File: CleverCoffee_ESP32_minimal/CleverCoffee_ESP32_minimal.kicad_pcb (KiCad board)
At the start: 2 copper layers, 78.2 x 57.5 mm, 24 parts

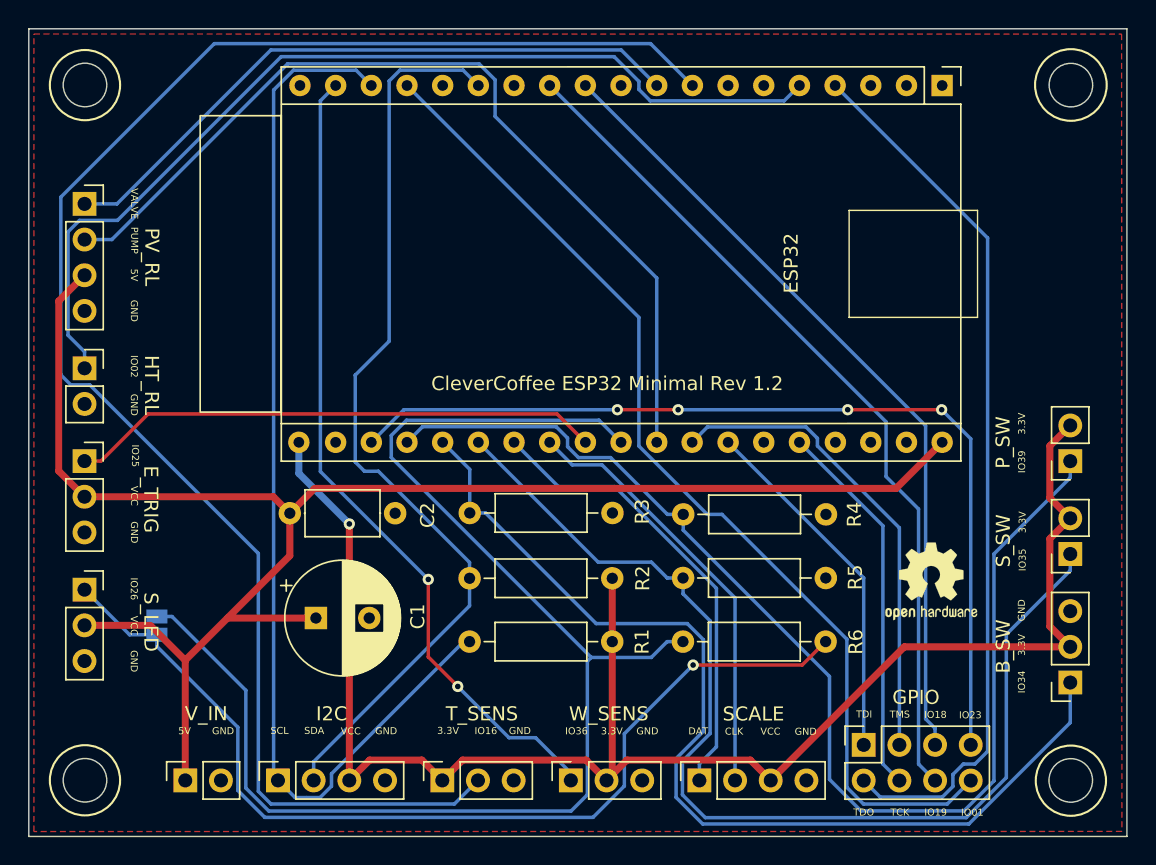
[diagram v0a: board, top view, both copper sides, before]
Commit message: Bugfix Labels Silkscreen
S_LED change VCC to 5V
E_TRIG change VCC to 5V
W_SENS change IO36 to IO23
GPIO change IO23 to IO36
change all VCC to 3,3V
change GPIO to IO Nummer
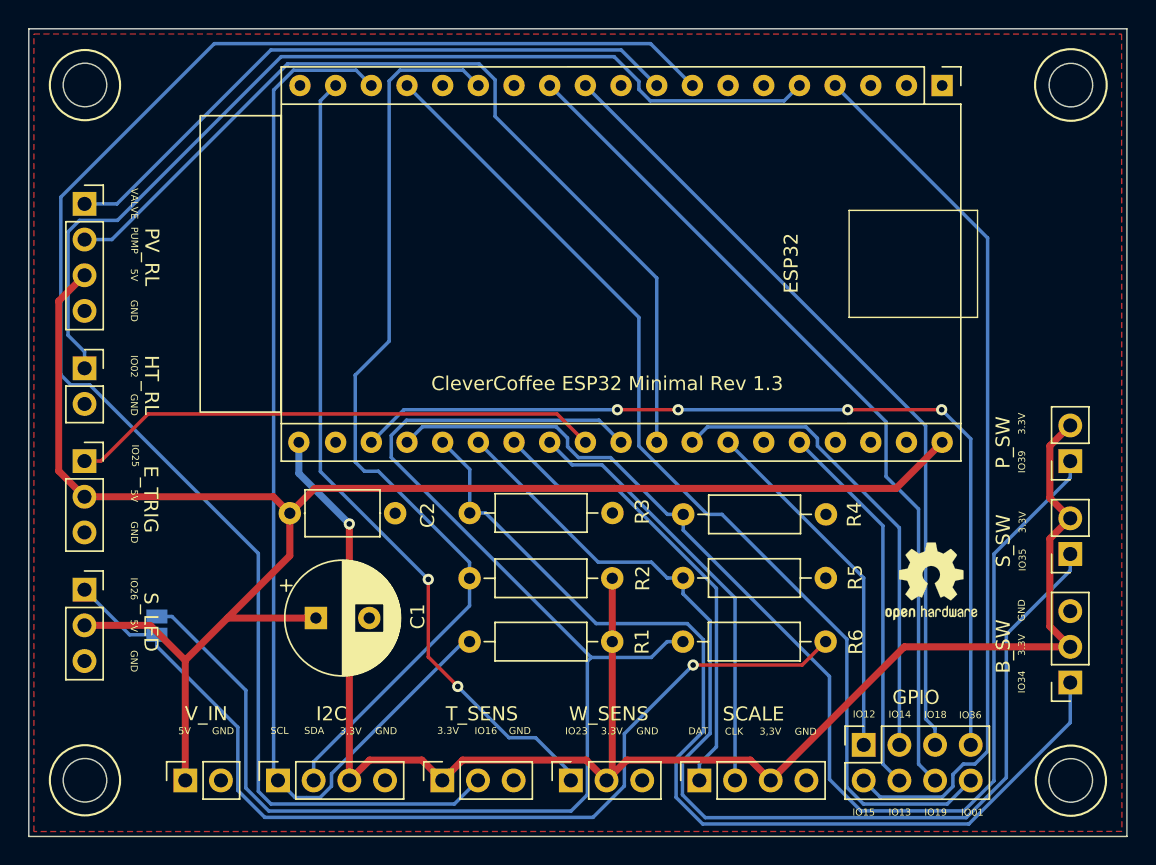
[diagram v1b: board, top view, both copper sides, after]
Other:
- board text added: "3,3V"
- board text added: "CleverCoffee ESP32 Minimal Rev 1.3"
- board text added: "IO12"
- board text added: "IO13"
- board text added: "IO14"
- board text added: "IO15"
- board text removed: "CleverCoffee ESP32 Minimal Rev 1.2"
- board text removed: "TCK"
- board text removed: "TDI"
- board text removed: "TDO"
- board text removed: "TMS"
- board text removed: "VCC"
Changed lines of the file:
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@@
       (connect_pads (clearance 0))
       (min_thickness 0.254)
-      (keepout (tracks not_allowed) (vias not_allowed) (pads not_allowed ) (copperpour allowed) (footprints allowed))
+      (keepout (tracks not_allowed) (vias not_allowed) (pads not_allowed) (copperpour allowed) (footprints allowed))
       (fill (thermal_gap 0.508) (thermal_bridge_width 0.508))
       (polygon
@@
   (gr_circle (center 173.99 79) (end 175.54 79) (layer "Edge.Cuts") (width 0.1) (fill none))
   (gr_circle (center 103.8 128.49) (end 105.35 128.49) (layer "Edge.Cuts") (width 0.1) (fill none))
-  (gr_text "TDO\n" (at 159.24 130.77) (layer "F.SilkS")
+  (gr_text "IO15\n" (at 159.24 130.77) (layer "F.SilkS")
     (effects (font (size 0.5 0.5) (thickness 0.1)))
   )
@@
     (effects (font (size 0.5 0.5) (thickness 0.1)))
   )
-  (gr_text "VCC" (at 107.29 117.49 270) (layer "F.SilkS")
+  (gr_text "5V" (at 107.29 117.49 270) (layer "F.SilkS")
     (effects (font (size 0.5 0.5) (thickness 0.1)))
   )
@@
     (effects (font (size 0.5 0.5) (thickness 0.1)))
   )
-  (gr_text "VCC" (at 152.6 125.01) (layer "F.SilkS")
-    (effects (font (size 0.5 0.5) (thickness 0.1)))
-  )
-  (gr_text "TCK\n" (at 161.81 130.77) (layer "F.SilkS")
-    (effects (font (size 0.5 0.5) (thickness 0.1)))
-  )
-  (gr_text "TMS\n" (at 161.81 123.8) (layer "F.SilkS")
+  (gr_text "3,3V" (at 152.6 125.01) (layer "F.SilkS")
+    (effects (font (size 0.5 0.5) (thickness 0.1)))
+  )
+  (gr_text "IO13" (at 161.81 130.77) (layer "F.SilkS")
+    (effects (font (size 0.5 0.5) (thickness 0.1)))
+  )
+  (gr_text "IO14" (at 161.81 123.8) (layer "F.SilkS")
     (effects (font (size 0.5 0.5) (thickness 0.1)))
   )
@@
     (effects (font (size 0.5 0.5) (thickness 0.1)))
   )
-  (gr_text "CleverCoffee ESP32 Minimal Rev 1.2" (at 140.98 100.25) (layer "F.SilkS")
+  (gr_text "CleverCoffee ESP32 Minimal Rev 1.3" (at 140.98 100.25) (layer "F.SilkS")
     (effects (font (size 1 1) (thickness 0.15)))
   )
@@
     (effects (font (size 0.5 0.5) (thickness 0.1)))
   )
-  (gr_text "VCC" (at 107.31 108.24 270) (layer "F.SilkS")
-    (effects (font (size 0.5 0.5) (thickness 0.1)))
-  )
-  (gr_text "TDI\n" (at 159.27 123.79) (layer "F.SilkS")
-    (effects (font (size 0.5 0.5) (thickness 0.1)))
-  )
-  (gr_text "VCC" (at 122.72 124.99) (layer "F.SilkS")
+  (gr_text "5V" (at 107.31 108.24 270) (layer "F.SilkS")
+    (effects (font (size 0.5 0.5) (thickness 0.1)))
+  )
+  (gr_text "IO12\n" (at 159.27 123.79) (layer "F.SilkS")
+    (effects (font (size 0.5 0.5) (thickness 0.1)))
+  )
+  (gr_text "3,3V" (at 122.72 124.99) (layer "F.SilkS")
     (effects (font (size 0.5 0.5) (thickness 0.1)))
   )
@@
     (effects (font (size 0.5 0.5) (thickness 0.1)))
   )
-  (gr_text "IO23\n\n" (at 166.83 124.25) (layer "F.SilkS")
+  (gr_text "IO36\n\n" (at 166.83 124.25) (layer "F.SilkS")
     (effects (font (size 0.5 0.5) (thickness 0.1)))
   )
@@
     (effects (font (size 0.5 0.5) (thickness 0.1)))
   )
-  (gr_text "IO36\n\n" (at 138.79 125.39) (layer "F.SilkS")
-    (effects (font (size 0.5 0.5) (thickness 0.1)))
-  )
+  (gr_text "IO23\n\n" (at 138.79 125.39) (layer "F.SilkS")
+    (effects (font (size 0.5 0.5) (thickness 0.1)))
+  )
